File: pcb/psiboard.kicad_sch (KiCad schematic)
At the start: 11 parts, among them J2 BAT+, J3 BAT-

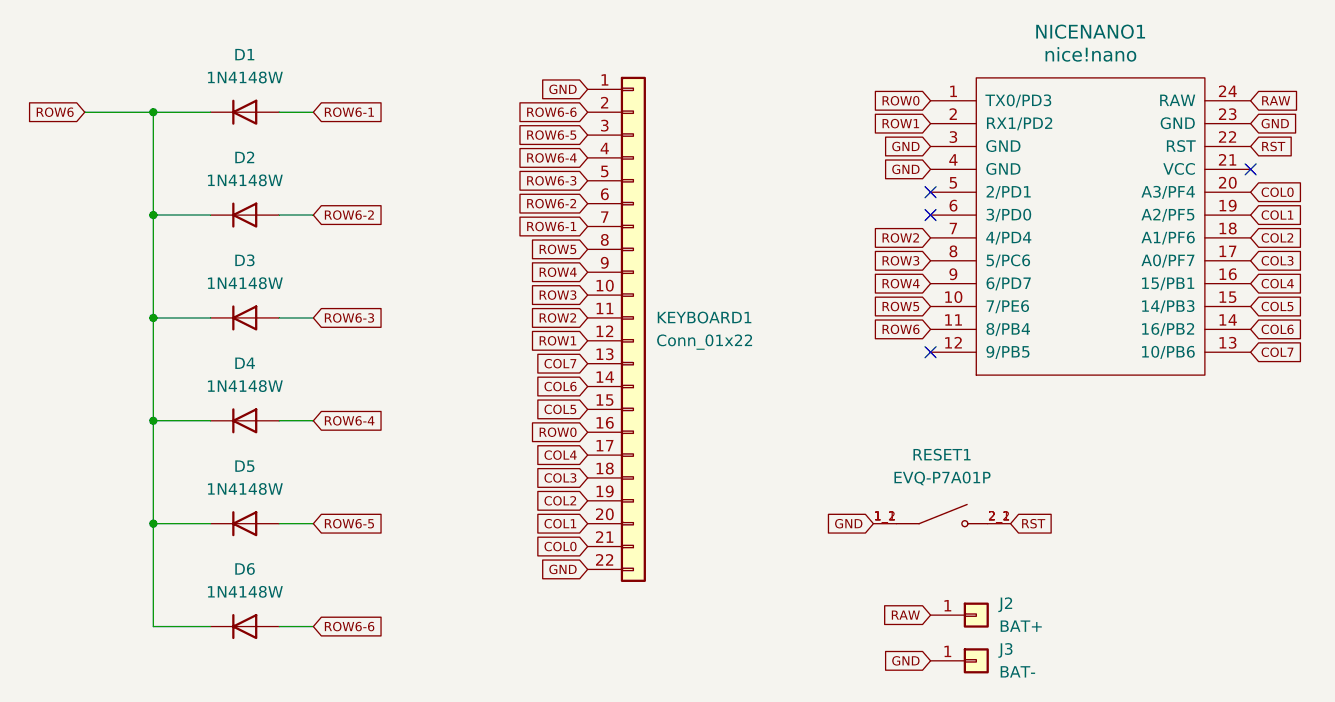
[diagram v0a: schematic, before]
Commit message: fix(pcb): Hand-route keyboard to simplify layout (#9)
This change also introduces a ground plane and makes the PCB
significantly larger to allow placement of a status LED in future
iterations.
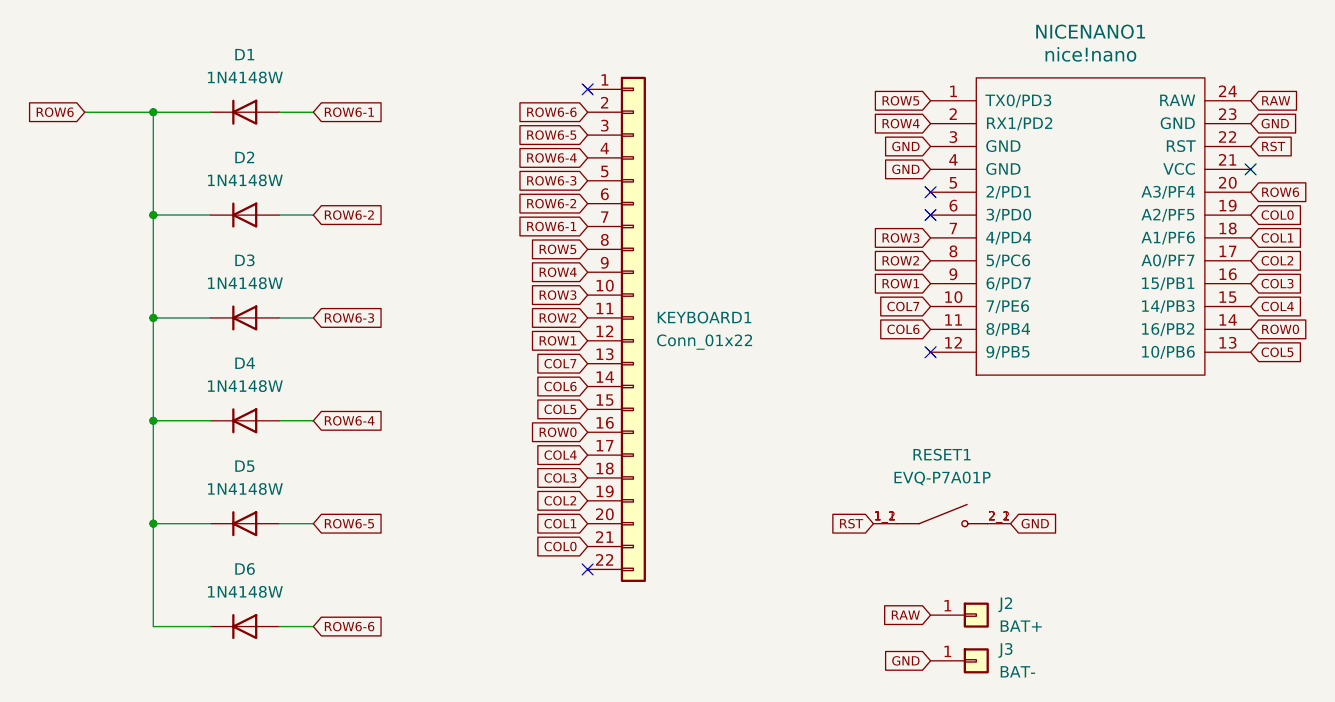
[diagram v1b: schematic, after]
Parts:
- KEYBOARD1: footprint 22-pin molex:CON_524352271_MOL -> 22-pin molex (bottom):CON_524372271_MOL
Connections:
- net COL0: now also NICENANO1.19 (A2/PF5); no longer NICENANO1.20 (A3/PF4)
- net COL1: now also NICENANO1.18 (A1/PF6); no longer NICENANO1.19 (A2/PF5)
- net COL2: now also NICENANO1.17 (A0/PF7); no longer NICENANO1.18 (A1/PF6)
- net COL3: now also NICENANO1.16 (15/PB1); no longer NICENANO1.17 (A0/PF7)
- net COL4: now also NICENANO1.15 (14/PB3); no longer NICENANO1.16 (15/PB1)
- net COL5: now also NICENANO1.13 (10/PB6); no longer NICENANO1.15 (14/PB3)
- net COL6: now also NICENANO1.11 (8/PB4); no longer NICENANO1.14 (16/PB2)
- net COL7: now also NICENANO1.10 (7/PE6); no longer NICENANO1.13 (10/PB6)
- net GND: now also RESET1.2_1, RESET1.2_2; no longer KEYBOARD1.1 (Pin_1), KEYBOARD1.22 (Pin_22), RESET1.1_1, RESET1.1_2
- net ROW0: now also NICENANO1.14 (16/PB2); no longer NICENANO1.1 (TX0/PD3)
- net ROW1: now also NICENANO1.9 (6/PD7); no longer NICENANO1.2 (RX1/PD2)
- net ROW2: now also NICENANO1.8 (5/PC6); no longer NICENANO1.7 (4/PD4)
- net ROW3: now also NICENANO1.7 (4/PD4); no longer NICENANO1.8 (5/PC6)
- net ROW4: now also NICENANO1.2 (RX1/PD2); no longer NICENANO1.9 (6/PD7)
- net ROW5: now also NICENANO1.1 (TX0/PD3); no longer NICENANO1.10 (7/PE6)
- net ROW6: now also NICENANO1.20 (A3/PF4); no longer NICENANO1.11 (8/PB4)
- net RST: now also RESET1.1_1, RESET1.1_2; no longer RESET1.2_1, RESET1.2_2
- no-connect marks 4 -> 6
